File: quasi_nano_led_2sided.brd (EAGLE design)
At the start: 40.3 x 58.4 mm, 4 parts, among them X1 JST-XH-02-PIN-LONG-PAD

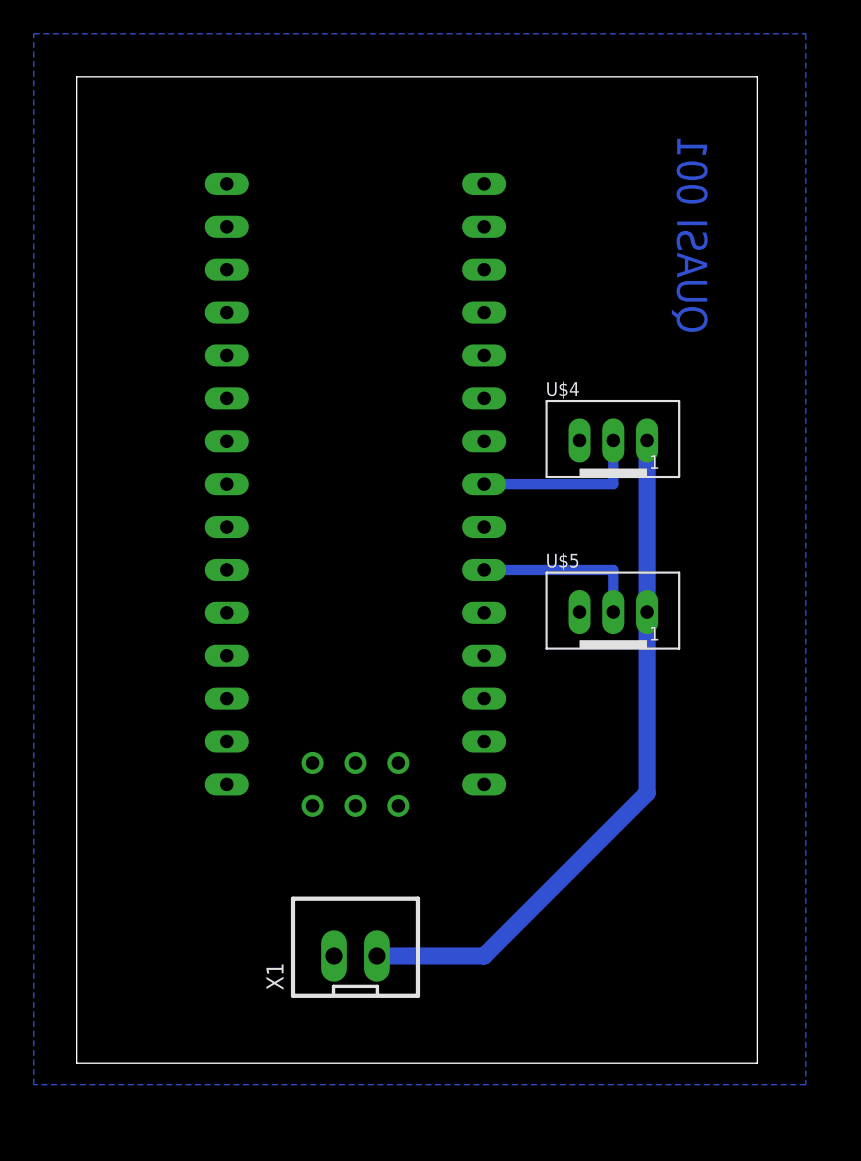
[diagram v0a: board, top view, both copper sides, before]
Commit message: add 4 wire board
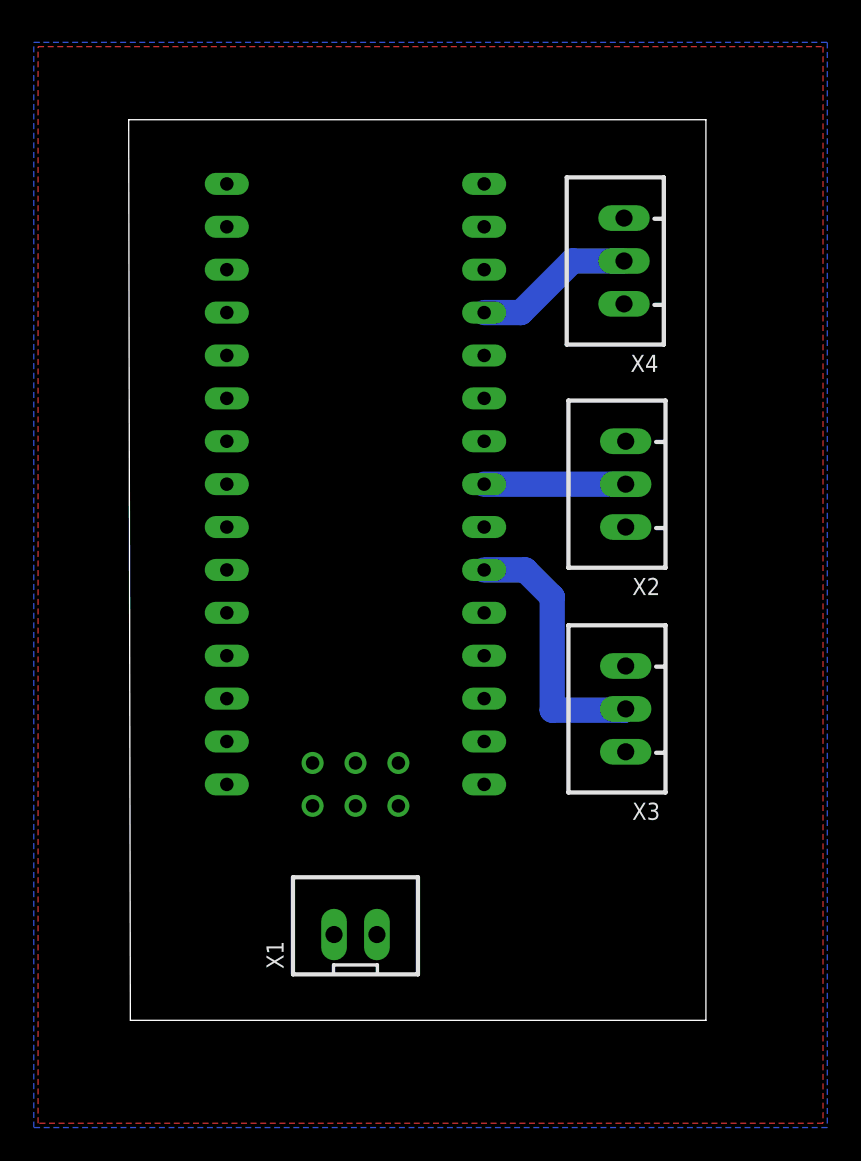
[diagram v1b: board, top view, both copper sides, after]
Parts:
- removed U$4, U$5: JST-PH_3-PIN_HEADER, con-jst-ph:JST_B3B-PH_HEADER
- added X2, X3, X4: JST-XH-03-PIN-LONG-PAD, Rembrandt Electronics - JST XH Connectors v1-0:JST-XH-03-PACKAGE-LONG-PAD
- moved X1 1.27 mm to (19.1, 29.2)
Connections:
- removed net N$4: U$4.P1, U$5.P1, X1.2
- new net 5V: X1.2, X2.1, X3.1, X4.1
- new net N$1: U$1.D9, X4.2
- net GND: now also X2.3, X3.3, X4.3; no longer U$4.P3, U$5.P3
- net N$6: now also X2.2; no longer U$4.P2
- net N$7: now also X3.2; no longer U$5.P2
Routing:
- net N$4: track 40.9 -> 0.00 mm
- net N$1: track 0.00 -> 9.55 mm
- net N$7: track 10.1 -> 15.8 mm
- net N$6: track 10.2 -> 8.38 mm
- added copper zone on layer 1, net 5V
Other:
- board size 40.3 x 58.4 mm -> 34.2 x 53.3 mm
- board text removed: "QUASI 001"
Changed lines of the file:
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@@
 <setting verticaltext="up"/>
 </settings>
-<grid distance="50" unitdist="mil" unit="mil" style="lines" multiple="1" display="no" altdistance="5" altunitdist="mil" altunit="mil"/>
+<grid distance="0.1" unitdist="mm" unit="mm" style="lines" multiple="10" display="yes" altdistance="5" altunitdist="mil" altunit="mm"/>
 <layers>
 <layer number="1" name="Top" color="4" fill="1" visible="yes" active="yes"/>
@@
 <board>
 <plain>
-<wire x1="2.54" y1="21.59" x2="42.85" y2="21.59" width="0" layer="20"/>
-<wire x1="42.85" y1="21.59" x2="42.85" y2="80" width="0" layer="20"/>
-<wire x1="42.85" y1="80" x2="2.54" y2="80" width="0" layer="20"/>
-<wire x1="2.54" y1="80" x2="2.54" y2="21.59" width="0" layer="20"/>
-<text x="38.1" y="64.77" size="1.778" layer="16" rot="MR90">QUASI 001</text>
+<wire x1="5.72" y1="24.13" x2="39.802" y2="24.13" width="0" layer="20"/>
+<wire x1="39.802" y1="24.13" x2="39.802" y2="77.46" width="0" layer="20"/>
+<wire x1="39.802" y1="77.46" x2="5.62" y2="77.46" width="0" layer="20"/>
+<wire x1="5.62" y1="77.46" x2="5.72" y2="24.13" width="0" layer="20"/>
 </plain>
 <attributes>
@@
 <elements>
 <element name="U$1" library="Arduino-clone" package="NANO" value="NANO" x="21.59" y="46.99" smashed="yes"/>
-<element name="U$4" library="con-jst-ph" package="JST_B3B-PH_HEADER" value="JST-PH_3-PIN_HEADER" x="34.29" y="58.42" smashed="yes">
-<attribute name="NAME" x="30.3175" y="61.1025" size="0.8128" layer="25" font="vector"/>
+<element name="X1" library="Rembrandt Electronics - JST XH Connectors v1-0" package="JST-XH-02-PACKAGE-LONG-PAD" value="JST-XH-02-PIN-LONG-PAD" x="19.05" y="29.21" smashed="yes">
+<attribute name="NAME" x="14.795" y="27.17" size="1.016" layer="25" ratio="10" rot="R90"/>
+<attribute name="VALUE" x="15.7475" y="33.1025" size="1.016" layer="27" ratio="10"/>
 </element>
-<element name="U$5" library="con-jst-ph" package="JST_B3B-PH_HEADER" value="JST-PH_3-PIN_HEADER" x="34.29" y="48.26" smashed="yes">
-<attribute name="NAME" x="30.3175" y="50.9425" size="0.8128" layer="25" font="vector"/>
+<element name="X2" library="Rembrandt Electronics - JST XH Connectors v1-0" package="JST-XH-03-PACKAGE-LONG-PAD" value="JST-XH-03-PIN-LONG-PAD" x="35.052" y="55.88" smashed="yes" rot="R90">
+<attribute name="NAME" x="37.092" y="50.325" size="1.016" layer="25" ratio="10" rot="R180"/>
+<attribute name="VALUE" x="31.1595" y="51.2775" size="1.016" layer="27" ratio="10" rot="R90"/>
 </element>
-<element name="X1" library="Rembrandt Electronics - JST XH Connectors v1-0" package="JST-XH-02-PACKAGE-LONG-PAD" value="JST-XH-02-PIN-LONG-PAD" x="19.05" y="27.94" smashed="yes">
-<attribute name="NAME" x="14.795" y="25.9" size="1.016" layer="25" ratio="10" rot="R90"/>
-<attribute name="VALUE" x="15.7475" y="31.8325" size="1.016" layer="27" ratio="10"/>
+<element name="X3" library="Rembrandt Electronics - JST XH Connectors v1-0" package="JST-XH-03-PACKAGE-LONG-PAD" value="JST-XH-03-PIN-LONG-PAD" x="35.052" y="42.572" smashed="yes" rot="R90">
+<attribute name="NAME" x="37.092" y="37.017" size="1.016" layer="25" ratio="10" rot="R180"/>
+<attribute name="VALUE" x="31.1595" y="37.9695" size="1.016" layer="27" ratio="10" rot="R90"/>
+</element>
+<element name="X4" library="Rembrandt Electronics - JST XH Connectors v1-0" package="JST-XH-03-PACKAGE-LONG-PAD" value="JST-XH-03-PIN-LONG-PAD" x="34.952" y="69.096" smashed="yes" rot="R90">
+<attribute name="NAME" x="36.992" y="63.541" size="1.016" layer="25" ratio="10" rot="R180"/>
+<attribute name="VALUE" x="31.0595" y="64.4935" size="1.016" layer="27" ratio="10" rot="R90"/>
 </element>
 </elements>
 <signals>
-<signal name="N$4">
-<contactref element="U$4" pad="P1"/>
-<contactref element="U$5" pad="P1"/>
-<contactref element="X1" pad="2"/>
-<wire x1="36.3175" y1="58.4675" x2="36.3175" y2="48.3075" width="1.016" layer="16"/>
-<wire x1="36.3175" y1="37.5875" x2="26.67" y2="27.94" width="1.016" layer="16"/>
-<wire x1="26.67" y1="27.94" x2="20.32" y2="27.94" width="1.016" layer="16"/>
-<wire x1="36.3175" y1="48.3075" x2="36.3175" y2="37.5875" width="1.016" layer="16"/>
-</signal>
 <signal name="N$6">
-<contactref element="U$4" pad="P2"/>
 <contactref element="U$1" pad="D5"/>
-<wire x1="26.67" y1="55.88" x2="34.3175" y2="55.88" width="0.6096" layer="16"/>
-<wire x1="34.3175" y1="55.88" x2="34.3175" y2="58.4675" width="0.6096" layer="16"/>
+<contactref element="X2" pad="2"/>
+<wire x1="26.67" y1="55.88" x2="35.052" y2="55.88" width="1.5" layer="16"/>
 </signal>
 <signal name="N$7">
 <contactref element="U$1" pad="D3"/>
-<contactref element="U$5" pad="P2"/>
-<wire x1="34.3175" y1="48.3075" x2="34.3175" y2="50.8" width="0.6096" layer="16"/>
-<wire x1="34.3175" y1="50.8" x2="26.67" y2="50.8" width="0.6096" layer="16"/>
+<contactref element="X3" pad="2"/>
+<wire x1="26.67" y1="50.8" x2="29.1" y2="50.8" width="1.5" layer="16"/>
+<wire x1="30.7" y1="49.2" x2="30.7" y2="42.5" width="1.5" layer="16"/>
+<wire x1="30.7" y1="42.5" x2="34.98" y2="42.5" width="1.5" layer="16"/>
+<wire x1="34.98" y1="42.5" x2="35.052" y2="42.572" width="1.5" layer="16"/>
+<wire x1="29.1" y1="50.8" x2="30.7" y2="49.2" width="1.5" layer="16"/>
 </signal>
 <signal name="GND">
-<polygon width="0.254" layer="16" isolate="0.8128">
-<vertex x="0" y="82.55"/>
-<vertex x="45.72" y="82.55"/>
-<vertex x="45.72" y="20.32"/>
-<vertex x="0" y="20.32"/>
+<polygon width="0.1524" layer="16" isolate="0.8128">
+<vertex x="0" y="82.042"/>
+<vertex x="46.99" y="82.042"/>
+<vertex x="46.99" y="17.78"/>
+<vertex x="0" y="17.78"/>
 </polygon>
 <contactref element="X1" pad="1"/>
 <contactref element="U$1" pad="GND"/>
-<contactref element="U$5" pad="P3"/>
-<contactref element="U$4" pad="P3"/>
 <contactref element="U$1" pad="GND1"/>
+<contactref element="X2" pad="3"/>
+<contactref element="X3" pad="3"/>
+<contactref element="X4" pad="3"/>
+</signal>
+<signal name="5V">
+<contactref element="X1" pad="2"/>
+<contactref element="X2" pad="1"/>
+<contactref element="X3" pad="1"/>
+<contactref element="X4" pad="1"/>
+<polygon width="0.1524" layer="1">
+<vertex x="0.254" y="18.034"/>
+<vertex x="0.254" y="81.788"/>
+<vertex x="46.736" y="81.788"/>
+<vertex x="46.736" y="18.034"/>
+</polygon>
+</signal>
+<signal name="N$1">
+<contactref element="X4" pad="2"/>
+<contactref element="U$1" pad="D9"/>
+<wire x1="26.67" y1="66.04" x2="28.84" y2="66.04" width="1.5" layer="16"/>
+<wire x1="31.896" y1="69.096" x2="34.952" y2="69.096" width="1.5" layer="16"/>
+<wire x1="28.84" y1="66.04" x2="31.896" y2="69.096" width="1.5" layer="16"/>
 </signal>
 </signals>
